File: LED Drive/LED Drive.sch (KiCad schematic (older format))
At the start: 0 parts

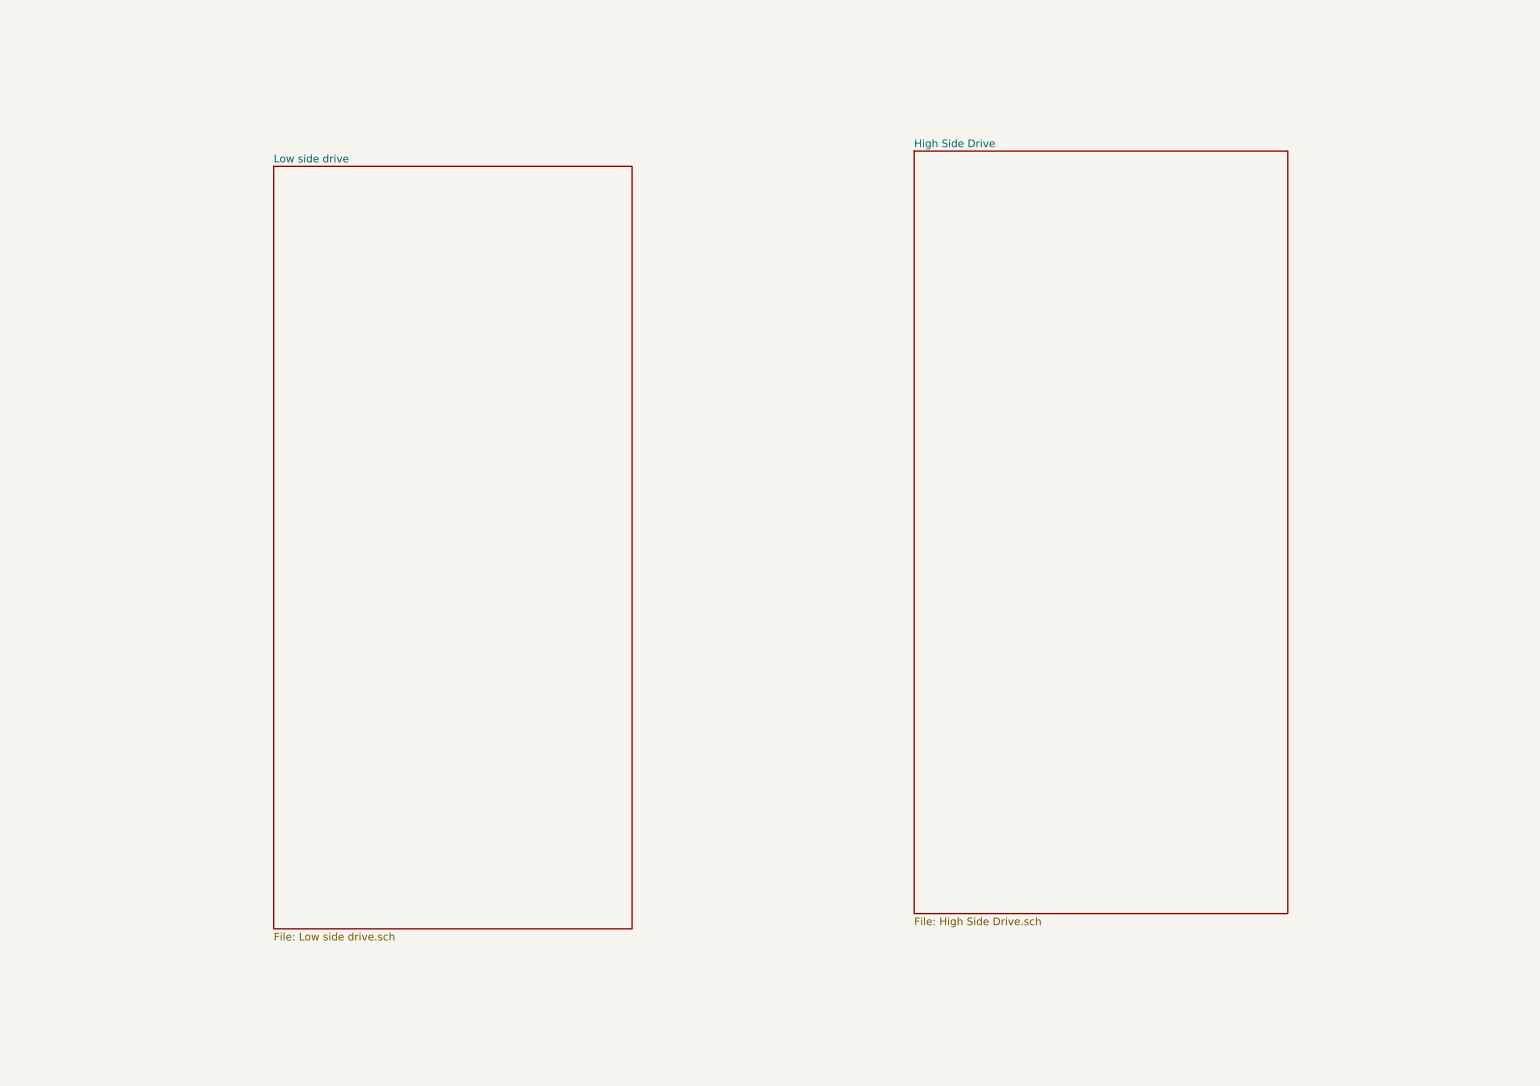
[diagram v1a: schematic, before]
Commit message: 9-4
Changing the LED drive to Opto-coupled
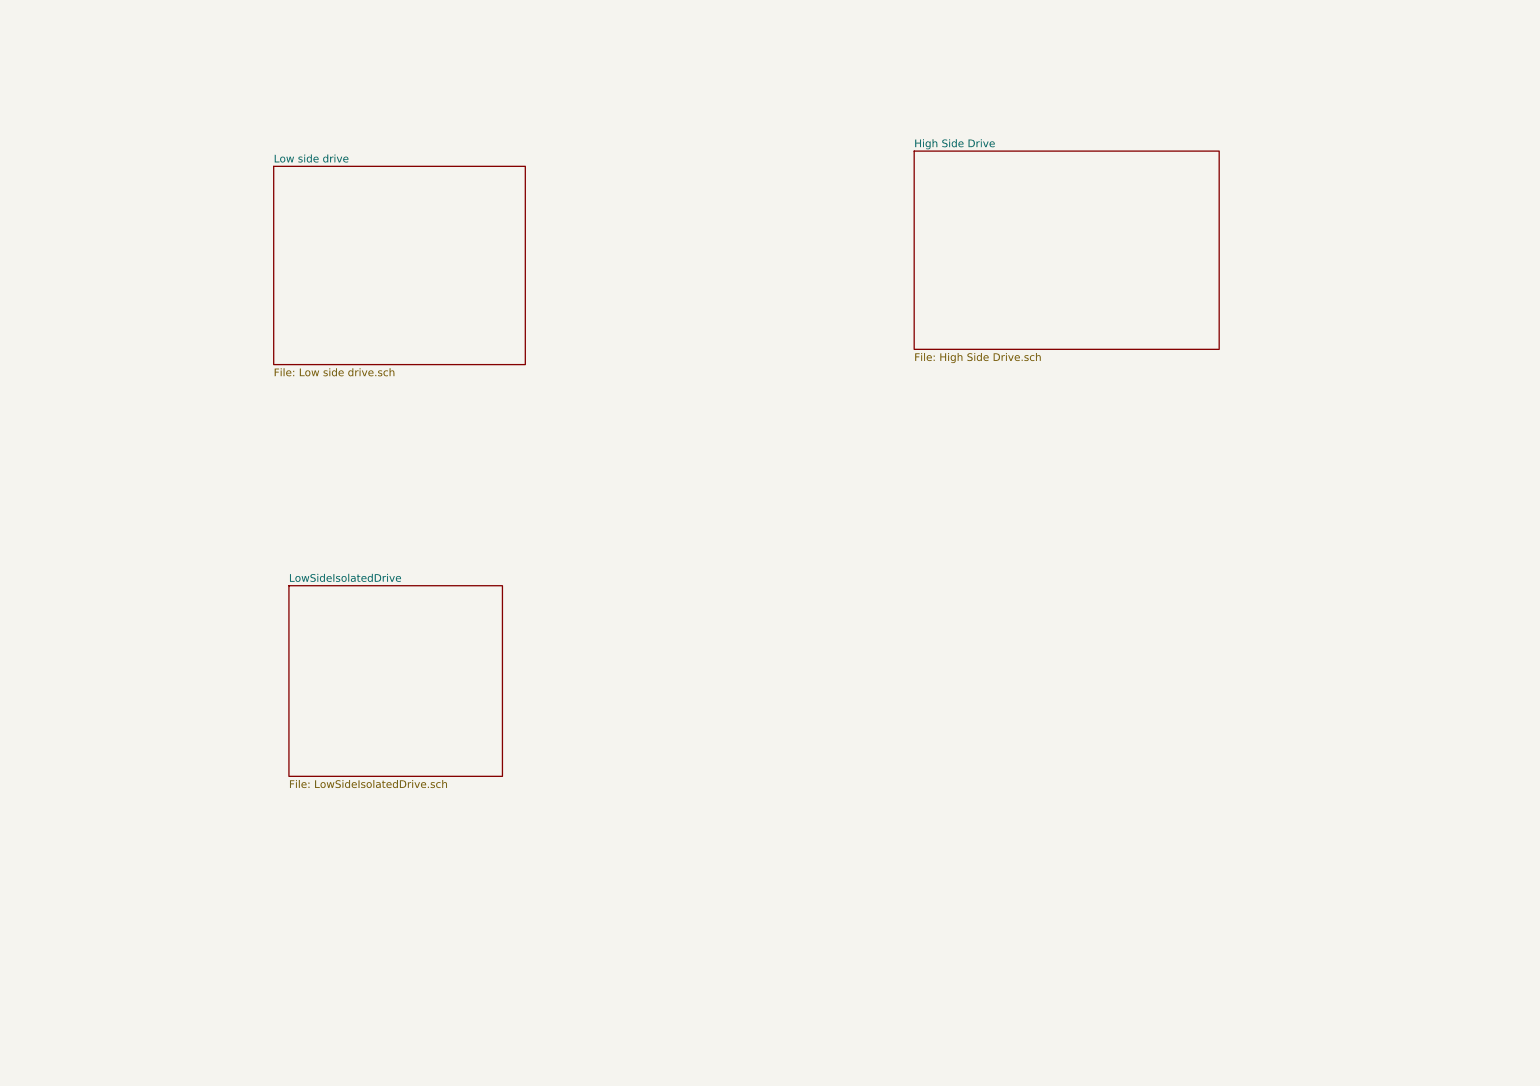
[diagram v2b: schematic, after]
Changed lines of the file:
@@
 $Descr A4 11693 8268
 encoding utf-8
-Sheet 1 3
+Sheet 1 4
 Title ""
-Date "4 sep 2014"
+Date "5 sep 2014"
 Rev ""
 Comp ""
@@
 $EndDescr
 $Sheet
-S 6750 1500 2450 5000
+S 6750 1500 2000 1300
 U 540394F4
 F0 "High Side Drive" 50
@@
 $EndSheet
 $Sheet
-S 2550 1600 2350 5000
+S 2550 1600 1650 1300
 U 54039517
 F0 "Low side drive" 50
 F1 "Low side drive.sch" 50
 $EndSheet
+$Sheet
+S 2650 4350 1400 1250
+U 54092826
+F0 "LowSideIsolatedDrive" 50
+F1 "LowSideIsolatedDrive.sch" 50
+$EndSheet
 $EndSCHEMATC

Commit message: 9-8
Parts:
- added U1: LOW_1-8, ~, symbol WIRE8
- added U2: LOW_9-16, ~, symbol WIRE8
- added U3: HIGH_1-8, ~, symbol WIRE8
- added U4: HIGH_9-16, ~, symbol WIRE8
- added U5: DATA, ~, symbol WIRE4
- added U6: 3.3V, ~, symbol WIRE2
- added U7: 12V, ~, symbol WIRE2
- added U8: DATA_OUT, ~, symbol WIRE2
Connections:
- new net 12V: U7.1
- new net 3.3V: U6.1
- new net CLK: U5.4
- new net GND1: U6.2
- new net GND2: U7.2
- new net HS_IN: U5.2
- new net HS_OUT: U8.2
- new net LS_IN: U5.1
- new net LS_OUT: U8.1
- new net SINK1: U1.1
- new net SINK10: U2.2
- new net SINK11: U2.3
- new net SINK12: U2.4
- new net SINK13: U2.5
- new net SINK14: U2.6
- new net SINK15: U2.7
- new net SINK16: U2.8
- new net SINK2: U1.2
- new net SINK3: U1.3
- new net SINK4: U1.4
- new net SINK5: U1.5
- new net SINK6: U1.6
- new net SINK7: U1.7
- new net SINK8: U1.8
- new net SINK9: U2.1
- new net SOURCE1: U3.1
- new net SOURCE10: U4.2
- new net SOURCE11: U4.3
- new net SOURCE12: U4.4
- new net SOURCE13: U4.5
- new net SOURCE14: U4.6
- new net SOURCE15: U4.7
- new net SOURCE16: U4.8
- new net SOURCE2: U3.2
- new net SOURCE3: U3.3
- new net SOURCE4: U3.4
- new net SOURCE5: U3.5
- new net SOURCE6: U3.6
- new net SOURCE7: U3.7
- new net SOURCE8: U3.8
- new net SOURCE9: U4.1
- new net STROBE: U5.3

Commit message: 9-16
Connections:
- net 3.3V renamed VCC3.3
- net GND1 renamed GND
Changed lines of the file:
@@
 Sheet 1 3
 Title ""
-Date "9 sep 2014"
+Date "10 sep 2014"
 Rev ""
 Comp ""
@@
 HS_IN
 Text GLabel 3150 2550 0    60   Input ~ 0
-3.3V
-Text GLabel 3150 2850 0    60   Input ~ 0
-GND1
+VCC3.3
 Text GLabel 3150 3700 0    60   Input ~ 0
 12V
-Text GLabel 3150 4000 0    60   Input ~ 0
-GND2
 Text GLabel 3100 4800 0    60   Input ~ 0
 LS_OUT
@@
 	3150 2550 3250 2550
 Wire Wire Line
-	3250 2850 3150 2850
+	2950 2850 3250 2850
+$Comp
+L GND #PWR01
+U 1 1 540FC021
+P 2950 2950
+F 0 "#PWR01" H 2950 2950 30  0001 C CNN
+F 1 "GND" H 2950 2880 30  0001 C CNN
+F 2 "" H 2950 2950 60  0000 C CNN
+F 3 "" H 2950 2950 60  0000 C CNN
+	1    2950 2950
+	1    0    0    -1
+$EndComp
+Wire Wire Line
+	2950 2850 2950 2950
+Text GLabel 3150 4000 0    60   Input ~ 0
+GND2
 $EndSCHEMATC
